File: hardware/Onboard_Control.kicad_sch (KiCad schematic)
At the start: 0 parts

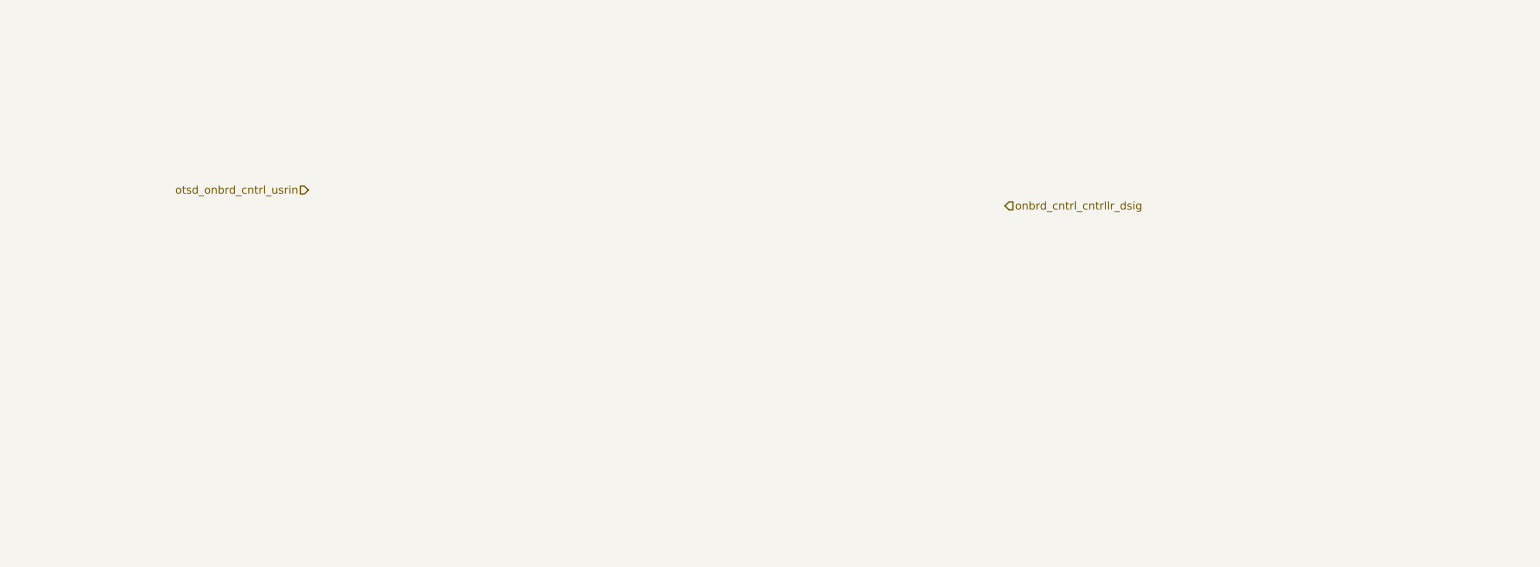
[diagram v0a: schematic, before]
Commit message: feat: button input initial
Added initial design for buttons on the PCB
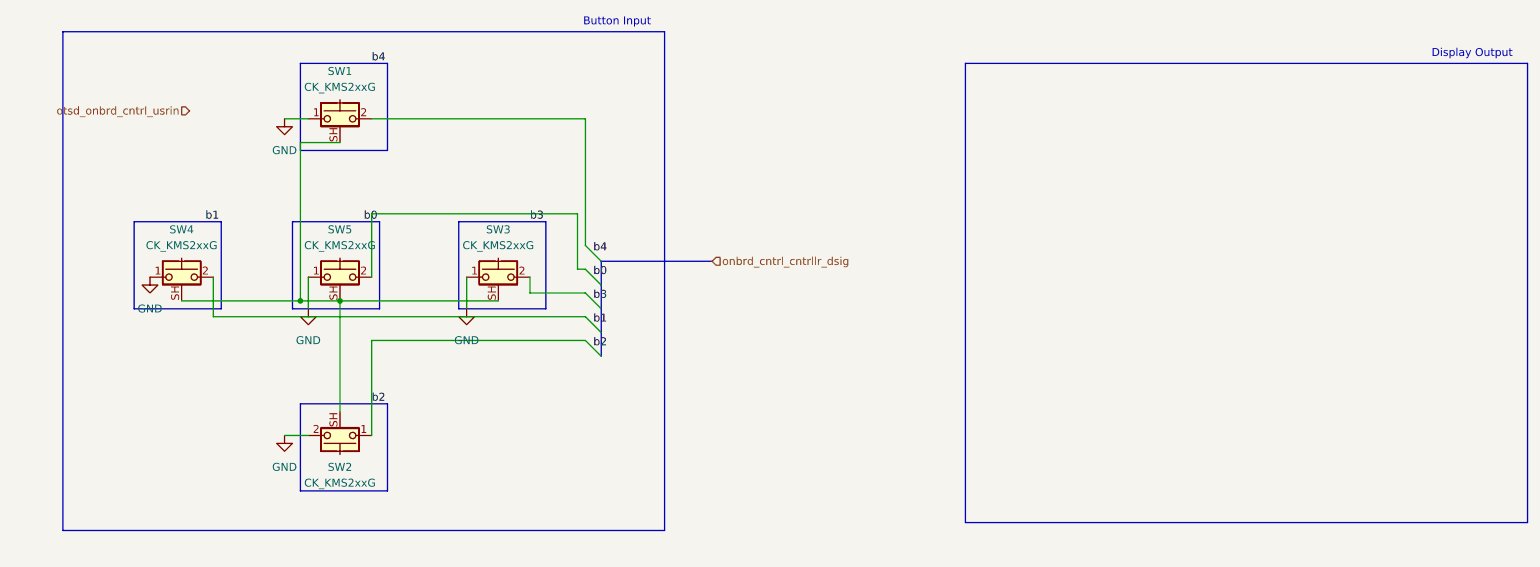
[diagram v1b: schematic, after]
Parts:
- added SW1, SW2, SW3, SW4, SW5: CK_KMS2xxG, Button_Switch_SMD:SW_SPST_CK_KMS2xxGP, symbol Switch:CK_KMS2xxG
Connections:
- new net: SW1.SH (B), SW2.SH (B), SW3.SH (B), SW4.SH (B), SW5.SH (B)
- new net GND: SW1.1, SW2.2, SW3.1, SW4.1, SW5.1
- new net b2: SW2.1
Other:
- note added: "Button Input"
- note added: "Display Output"

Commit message: chore: update project references
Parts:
- renumbered SW4 to SW8001, SW1 to SW8002, SW5 to SW8003, SW2 to SW8004, SW3 to SW8005
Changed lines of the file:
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@@
 		(dnp no)
 		(fields_autoplaced yes)
-		(property "Reference" "#PWR05"
+		(property "Reference" "#PWR08004"
 			(at 59.69 114.3 0)
 			(effects
@@
 			(project "gpu-external-power-supply"
 				(path "/d5303413-7068-41ba-88e3-39dfa38d31b7/5068f4fb-295f-4c02-a1ca-8a4133aa46e7"
-					(reference "#PWR05")
+					(reference "#PWR08004")
 					(unit 1)
 				)
@@
 		(dnp no)
 		(fields_autoplaced yes)
-		(property "Reference" "SW4"
+		(property "Reference" "SW8001"
 			(at 39.37 95.25 0)
 			(effects
@@
 			(project "gpu-external-power-supply"
 				(path "/d5303413-7068-41ba-88e3-39dfa38d31b7/5068f4fb-295f-4c02-a1ca-8a4133aa46e7"
-					(reference "SW4")
+					(reference "SW8001")
 					(unit 1)
 				)
@@
 		(dnp no)
 		(fields_autoplaced yes)
-		(property "Reference" "#PWR04"
+		(property "Reference" "#PWR08001"
 			(at 34.29 109.22 0)
 			(effects
@@
 			(project "gpu-external-power-supply"
 				(path "/d5303413-7068-41ba-88e3-39dfa38d31b7/5068f4fb-295f-4c02-a1ca-8a4133aa46e7"
-					(reference "#PWR04")
+					(reference "#PWR08001")
 					(unit 1)
 				)
@@
 		(dnp no)
 		(fields_autoplaced yes)
-		(property "Reference" "SW2"
+		(property "Reference" "SW8004"
 			(at 64.77 133.35 0)
 			(effects
@@
 			(project "gpu-external-power-supply"
 				(path "/d5303413-7068-41ba-88e3-39dfa38d31b7/5068f4fb-295f-4c02-a1ca-8a4133aa46e7"
-					(reference "SW2")
+					(reference "SW8004")
 					(unit 1)
 				)
@@
 		(dnp no)
 		(fields_autoplaced yes)
-		(property "Reference" "SW3"
+		(property "Reference" "SW8005"
 			(at 90.17 95.25 0)
 			(effects
@@
 			(project "gpu-external-power-supply"
 				(path "/d5303413-7068-41ba-88e3-39dfa38d31b7/5068f4fb-295f-4c02-a1ca-8a4133aa46e7"
-					(reference "SW3")
+					(reference "SW8005")
 					(unit 1)
 				)
@@
 		(dnp no)
 		(fields_autoplaced yes)
-		(property "Reference" "SW1"
+		(property "Reference" "SW8002"
 			(at 64.77 69.85 0)
 			(effects
@@
 			(project ""
 				(path "/d5303413-7068-41ba-88e3-39dfa38d31b7/5068f4fb-295f-4c02-a1ca-8a4133aa46e7"
-					(reference "SW1")
+					(reference "SW8002")
 					(unit 1)
 				)
@@
 		(dnp no)
 		(fields_autoplaced yes)
-		(property "Reference" "#PWR06"
+		(property "Reference" "#PWR08005"
 			(at 85.09 114.3 0)
 			(effects
@@
 			(project "gpu-external-power-supply"
 				(path "/d5303413-7068-41ba-88e3-39dfa38d31b7/5068f4fb-295f-4c02-a1ca-8a4133aa46e7"
-					(reference "#PWR06")
+					(reference "#PWR08005")
 					(unit 1)
 				)
@@
 		(dnp no)
 		(fields_autoplaced yes)
-		(property "Reference" "SW5"
+		(property "Reference" "SW8003"
 			(at 64.77 95.25 0)
 			(effects
@@
 			(project "gpu-external-power-supply"
 				(path "/d5303413-7068-41ba-88e3-39dfa38d31b7/5068f4fb-295f-4c02-a1ca-8a4133aa46e7"
-					(reference "SW5")
+					(reference "SW8003")
 					(unit 1)
 				)
@@
 		(dnp no)
 		(fields_autoplaced yes)
-		(property "Reference" "#PWR07"
+		(property "Reference" "#PWR08003"
 			(at 55.88 134.62 0)
 			(effects
@@
 			(project "gpu-external-power-supply"
 				(path "/d5303413-7068-41ba-88e3-39dfa38d31b7/5068f4fb-295f-4c02-a1ca-8a4133aa46e7"
-					(reference "#PWR07")
+					(reference "#PWR08003")
 					(unit 1)
 				)
@@
 		(dnp no)
 		(fields_autoplaced yes)
-		(property "Reference" "#PWR03"
+		(property "Reference" "#PWR08002"
 			(at 55.88 83.82 0)
 			(effects
@@
 			(project "gpu-external-power-supply"
 				(path "/d5303413-7068-41ba-88e3-39dfa38d31b7/5068f4fb-295f-4c02-a1ca-8a4133aa46e7"
-					(reference "#PWR03")
-					(unit 1)
-				)
+					(reference "#PWR08002")
+					(unit 1)
+				)

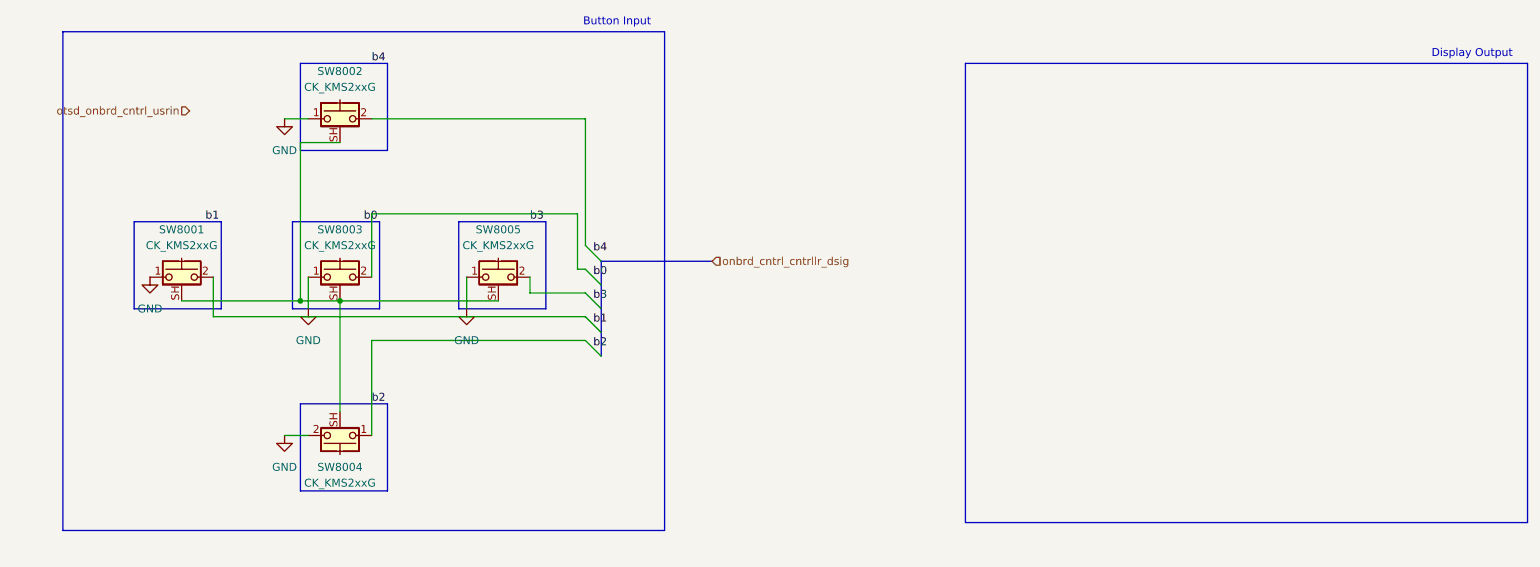
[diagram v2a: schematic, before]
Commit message: refactor(schematic): onboard control connect to microcontroller
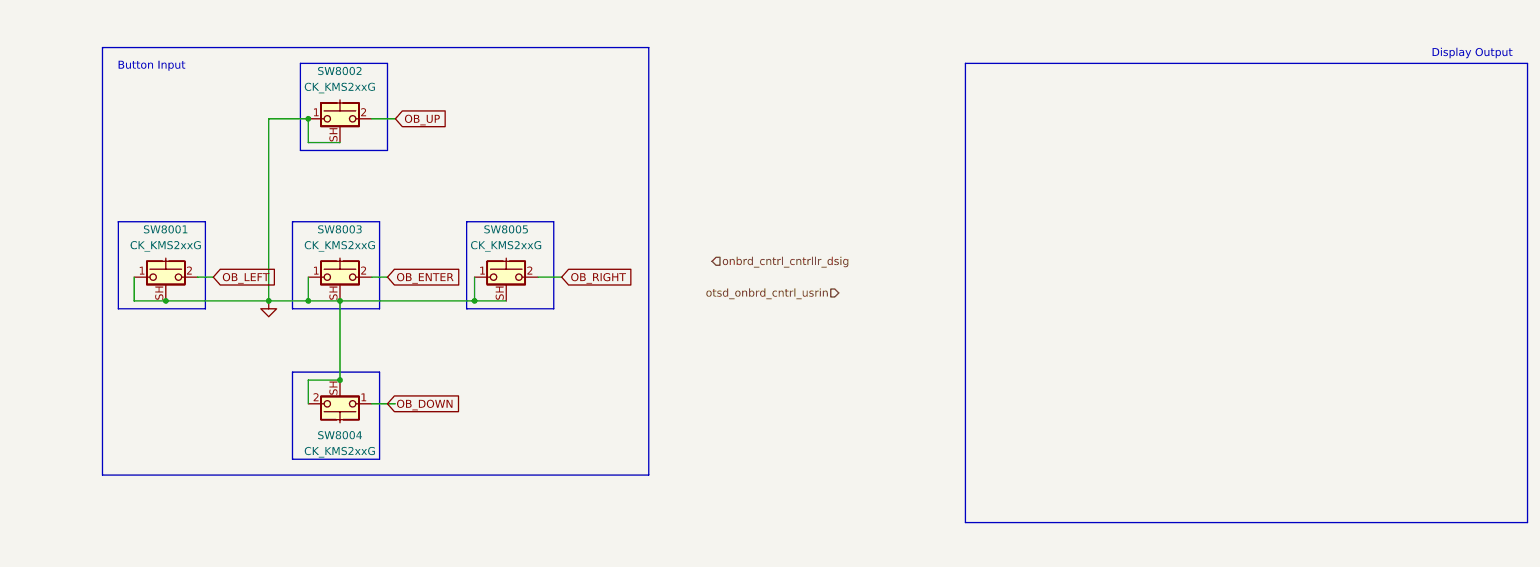
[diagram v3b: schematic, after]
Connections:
- net GND: now also SW8001.SH (B), SW8002.SH (B), SW8003.SH (B), SW8004.SH (B), SW8005.SH (B)
- net OB_LEFT: now reaches SW8001.2
- net OB_RIGHT: now reaches SW8005.2
- net OB_UP: now reaches SW8002.2
- net OB_ENTER: now reaches SW8003.2
- net b2 renamed OB_DOWN
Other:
- moved on the sheet: SW8001, SW8004, SW8005

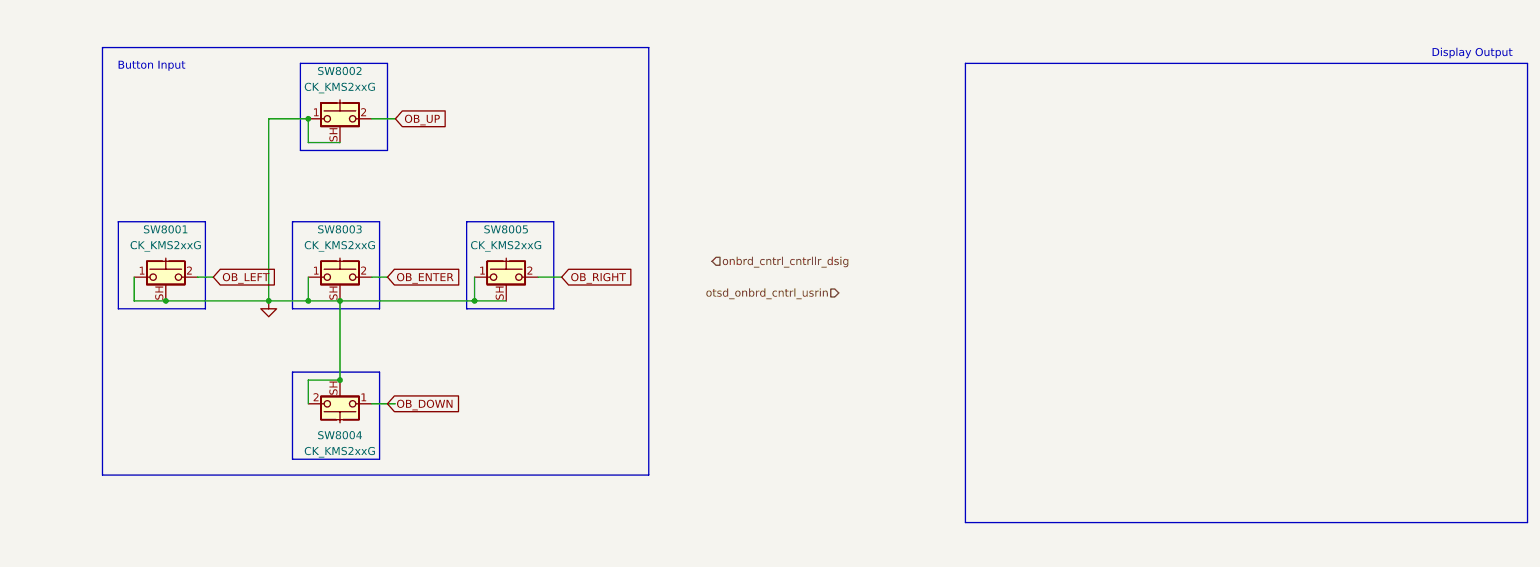
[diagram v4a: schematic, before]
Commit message: feat(schematic): add onboard display
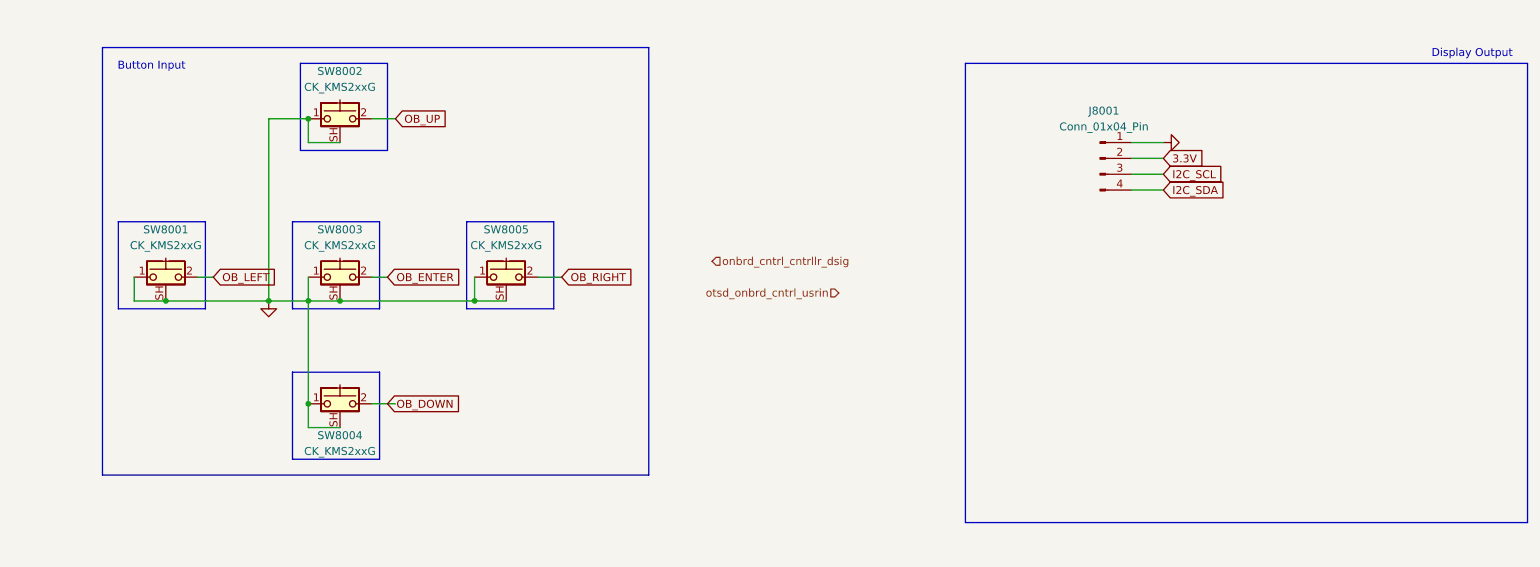
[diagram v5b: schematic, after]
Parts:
- added J8001: Conn_01x04_Pin, work:CONN_PPTC041LFBN-RC_SUL, symbol Connector:Conn_01x04_Pin
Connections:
- net GND: now also SW8004.1, J8001.1 (Pin_1); no longer SW8004.2
- net OB_DOWN: now also SW8004.2; no longer SW8004.1
- new net 3.3V: J8001.2 (Pin_2)
- new net I2C_SCL: J8001.3 (Pin_3)
- new net I2C_SDA: J8001.4 (Pin_4)
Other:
- moved on the sheet: SW8004

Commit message: fix(schematic): Minor Style changes to u controller and onboard control
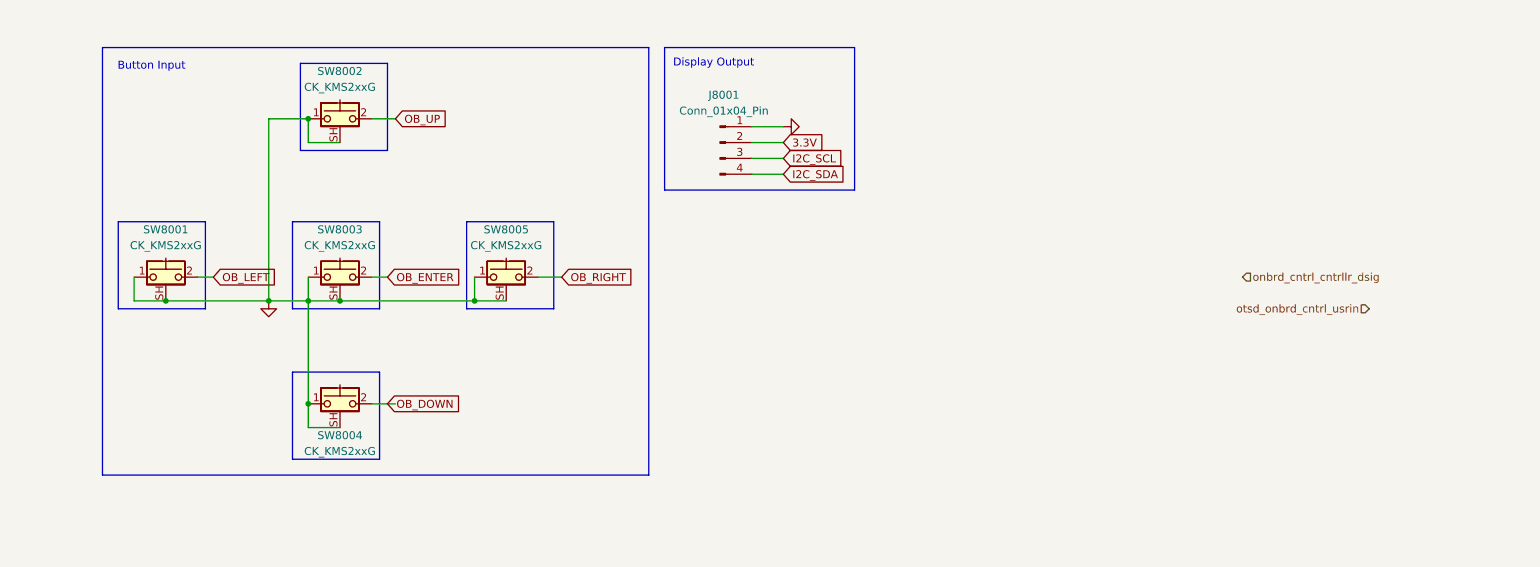
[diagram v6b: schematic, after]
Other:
- moved on the sheet: J8001
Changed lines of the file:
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@@
 	(wire
 		(pts
-			(xy 191.77 81.28) (xy 196.85 81.28)
+			(xy 130.81 78.74) (xy 135.89 78.74)
 		)
 		(stroke
@@
 	(wire
 		(pts
-			(xy 191.77 88.9) (xy 196.85 88.9)
+			(xy 130.81 86.36) (xy 135.89 86.36)
 		)
 		(stroke
@@
 	(wire
 		(pts
-			(xy 191.77 86.36) (xy 196.85 86.36)
+			(xy 130.81 83.82) (xy 135.89 83.82)
 		)
 		(stroke
@@
 	(wire
 		(pts
-			(xy 191.77 83.82) (xy 196.85 83.82)
+			(xy 130.81 81.28) (xy 135.89 81.28)
 		)
 		(stroke
@@
 	)
 	(rectangle
-		(start 165.1 68.58)
-		(end 255.27 142.24)
+		(start 116.84 66.04)
+		(end 147.32 88.9)
 		(stroke
 			(width 0)
@@
 	(text "Display Output"
 		(exclude_from_sim no)
-		(at 246.38 67.056 0)
+		(at 124.714 68.58 0)
 		(effects
 			(font
@@
 	(global_label "I2C_SCL"
 		(shape input)
-		(at 196.85 86.36 0)
+		(at 135.89 83.82 0)
 		(fields_autoplaced yes)
 		(effects
@@
 		)
 		(property "Intersheetrefs" "${INTERSHEET_REFS}"
-			(at 207.3947 86.36 0)
+			(at 146.4347 83.82 0)
 			(effects
 				(font
@@
 	(global_label "3.3V"
 		(shape input)
-		(at 196.85 83.82 0)
+		(at 135.89 81.28 0)
 		(fields_autoplaced yes)
 		(effects
@@
 		)
 		(property "Intersheetrefs" "${INTERSHEET_REFS}"
-			(at 203.9476 83.82 0)
+			(at 142.9876 81.28 0)
 			(effects
 				(font
@@
 	(global_label "I2C_SDA"
 		(shape input)
-		(at 196.85 88.9 0)
+		(at 135.89 86.36 0)
 		(fields_autoplaced yes)
 		(effects
@@
 		)
 		(property "Intersheetrefs" "${INTERSHEET_REFS}"
-			(at 207.4552 88.9 0)
+			(at 146.4952 86.36 0)
 			(effects
 				(font
@@
 	(hierarchical_label "onbrd_cntrl_cntrllr_dsig"
 		(shape input)
-		(at 124.46 100.33 0)
+		(at 209.55 102.87 0)
 		(fields_autoplaced yes)
 		(effects
@@
 	(hierarchical_label "otsd_onbrd_cntrl_usrin"
 		(shape input)
-		(at 144.78 105.41 180)
+		(at 229.87 107.95 180)
 		(fields_autoplaced yes)
 		(effects
@@
 	(symbol
 		(lib_id "power:GND")
-		(at 196.85 81.28 90)
+		(at 135.89 78.74 90)
 		(unit 1)
 		(exclude_from_sim no)
@@
 		(fields_autoplaced yes)
 		(property "Reference" "#PWR08001"
-			(at 203.2 81.28 0)
+			(at 142.24 78.74 0)
 			(effects
 				(font
@@
 		)
 		(property "Value" "GND"
-			(at 200.66 81.2799 90)
+			(at 139.7 78.7399 90)
 			(effects
 				(font
@@
 		)
 		(property "Footprint" ""
-			(at 196.85 81.28 0)
+			(at 135.89 78.74 0)
 			(effects
 				(font
@@
 		)
 		(property "Datasheet" ""
-			(at 196.85 81.28 0)
+			(at 135.89 78.74 0)
 			(effects
 				(font
@@
 		)
 		(property "Description" "Power symbol creates a global label with name \"GND\" , ground"
-			(at 196.85 81.28 0)
+			(at 135.89 78.74 0)
 			(effects
 				(font
@@
 	(symbol
 		(lib_id "Connector:Conn_01x04_Pin")
-		(at 186.69 83.82 0)
+		(at 125.73 81.28 0)
 		(unit 1)
 		(exclude_from_sim no)
@@
 		(fields_autoplaced yes)
 		(property "Reference" "J8001"
-			(at 187.325 76.2 0)
+			(at 126.365 73.66 0)
 			(effects
 				(font
@@
 		)
 		(property "Value" "Conn_01x04_Pin"
-			(at 187.325 78.74 0)
+			(at 126.365 76.2 0)
 			(effects
 				(font
@@
 		)
 		(property "Footprint" "work:CONN_PPTC041LFBN-RC_SUL"
-			(at 186.69 83.82 0)
+			(at 125.73 81.28 0)
 			(effects
 				(font
@@
 		)
 		(property "Datasheet" "https://www.digikey.com/en/products/detail/sullins-connector-solutions/PPTC041LFBN-RC/810144"
-			(at 186.69 83.82 0)
+			(at 125.73 81.28 0)
 			(effects
 				(font
@@
 		)
 		(property "Description" "Generic connector, single row, 01x04, script generated"
-			(at 186.69 83.82 0)
-			(effects
-				(font
+			(at 125.73 81.28 0)
+			(effects
+				(font
